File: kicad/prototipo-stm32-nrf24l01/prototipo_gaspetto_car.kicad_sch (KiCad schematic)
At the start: 11 parts, among them J1 Conn_01x07_Pin - TEST POINT, M1 Motor_DC, M2 Motor_DC, Q1 BC548, U1 YAAJ_BluePill_Part_Like_SWD_B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, U2 nRF24L01+, U3 L9110-M1, U4 L9110-M2

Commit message: kicad: clean projects
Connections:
- net at U1.12 (PB4): no longer U2.4 (CSN)
- net at U1.29 (PA4): now also U2.4 (CSN)
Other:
- moved on the sheet: PS1, PS2

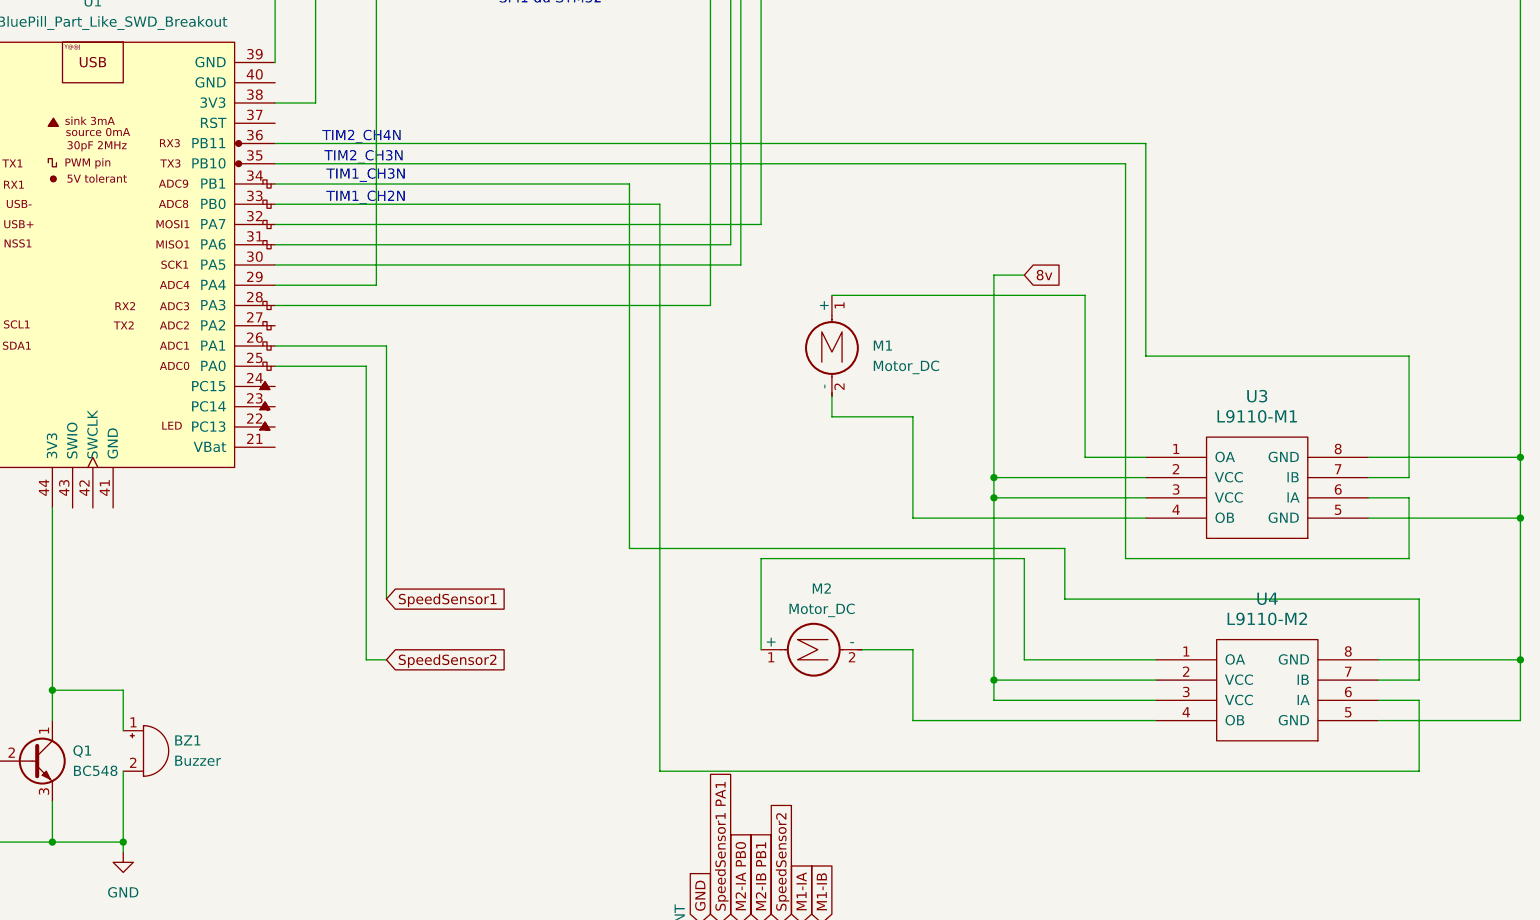
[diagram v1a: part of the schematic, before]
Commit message: sch: gaspetto car match with what's in the board
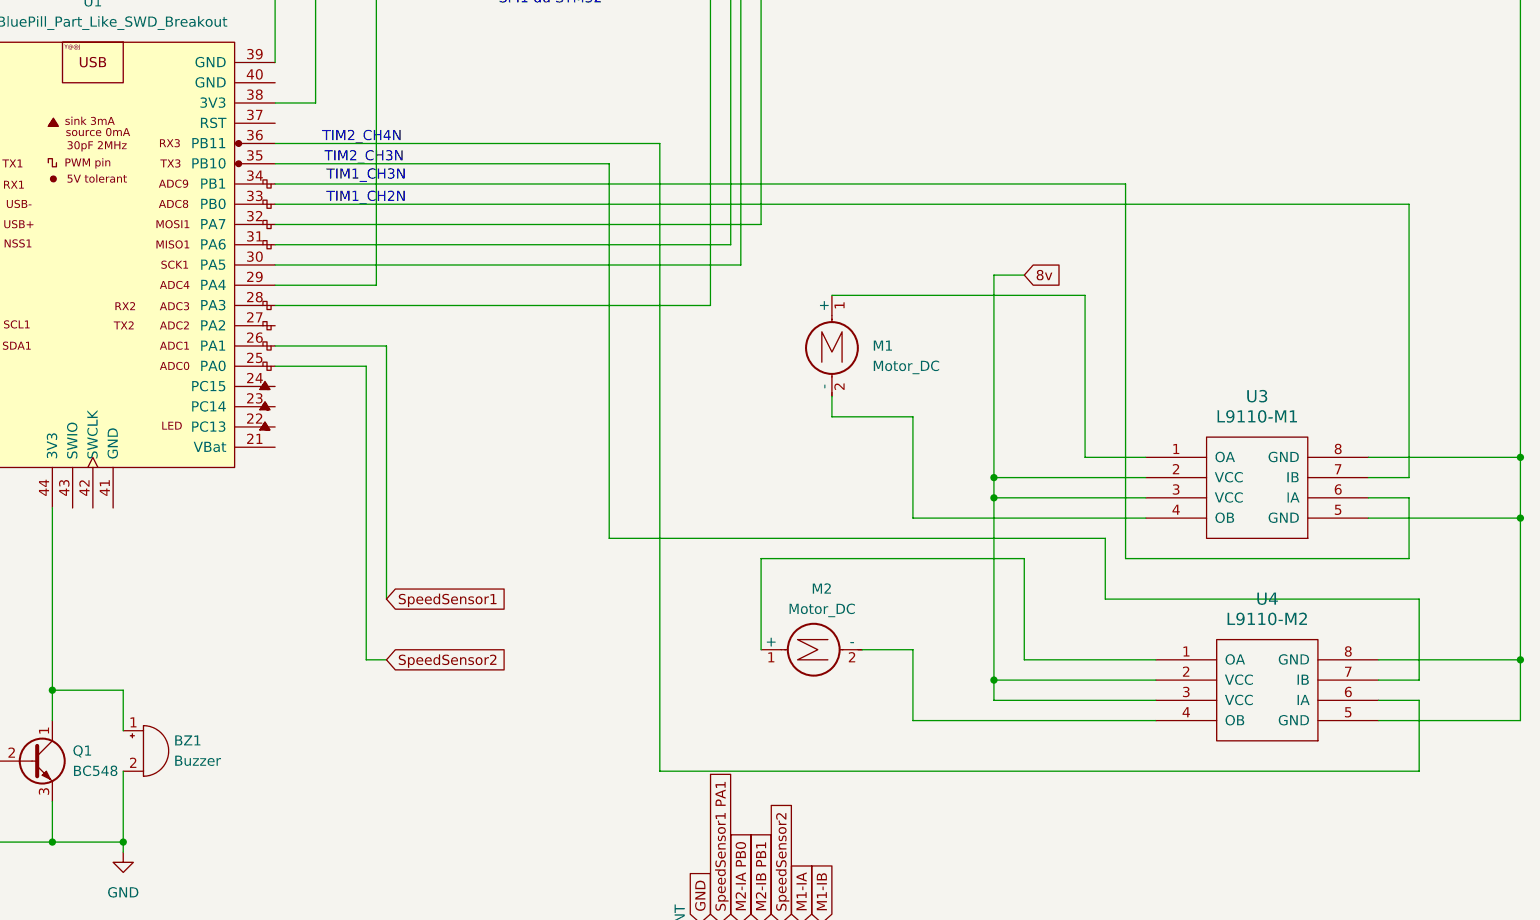
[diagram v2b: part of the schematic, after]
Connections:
- net at U1.33 (PB0): now also U3.7 (IB); no longer U4.6 (IA)
- net at U1.34 (PB1): now also U3.6 (IA); no longer U4.7 (IB)
- net at U1.35 (PB10): now also U4.7 (IB); no longer U3.6 (IA)
- net at U1.36 (PB11): now also U4.6 (IA); no longer U3.7 (IB)

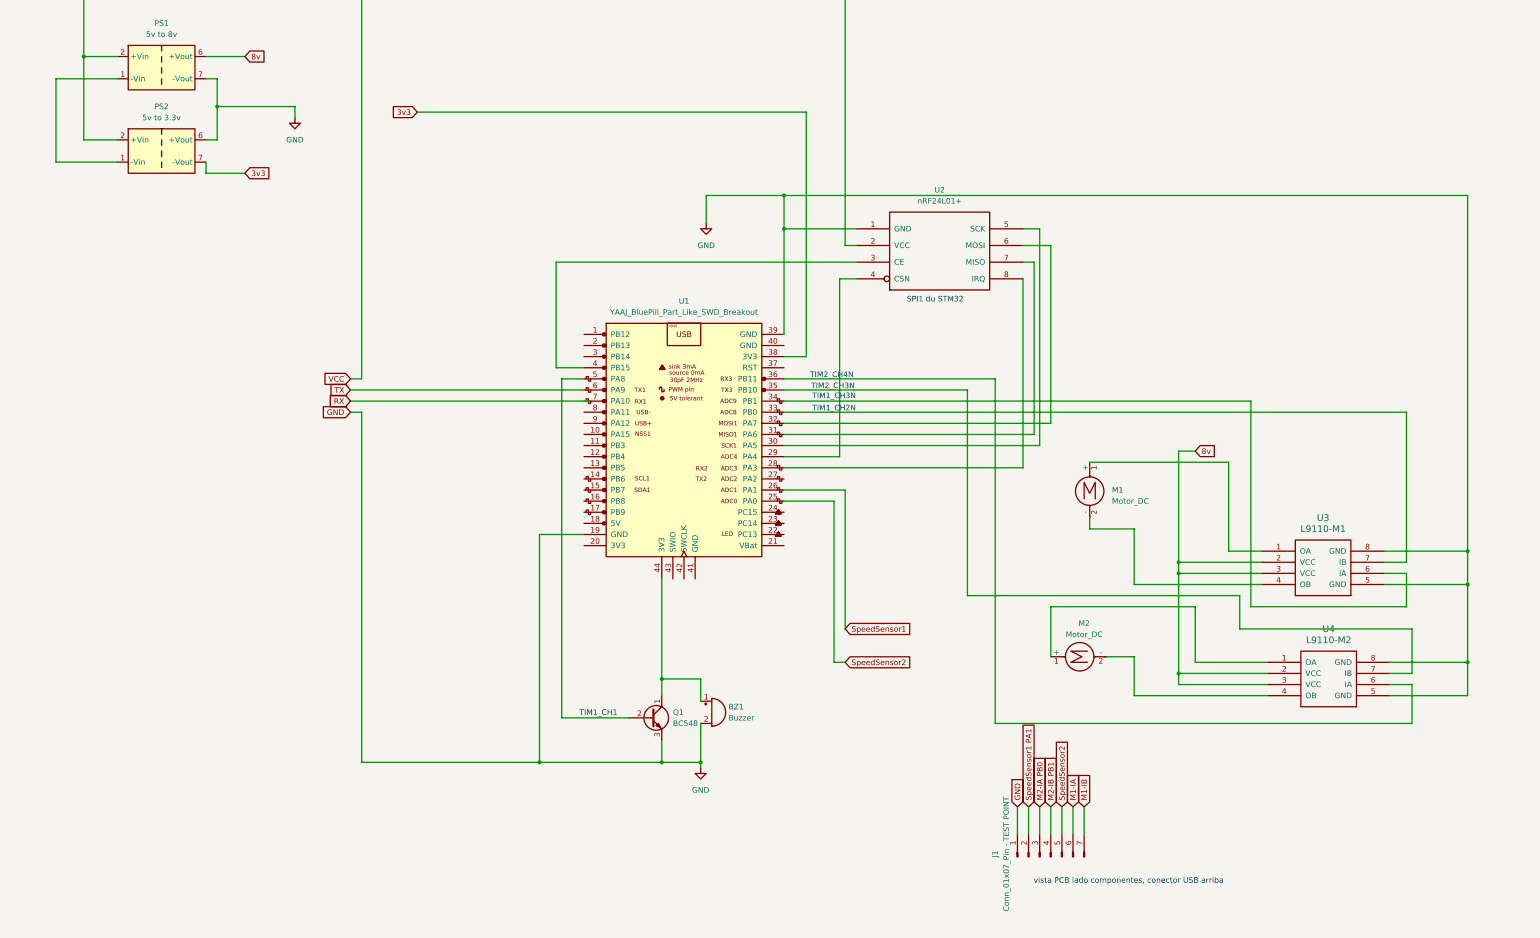
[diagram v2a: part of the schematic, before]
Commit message: sch car: update schematic
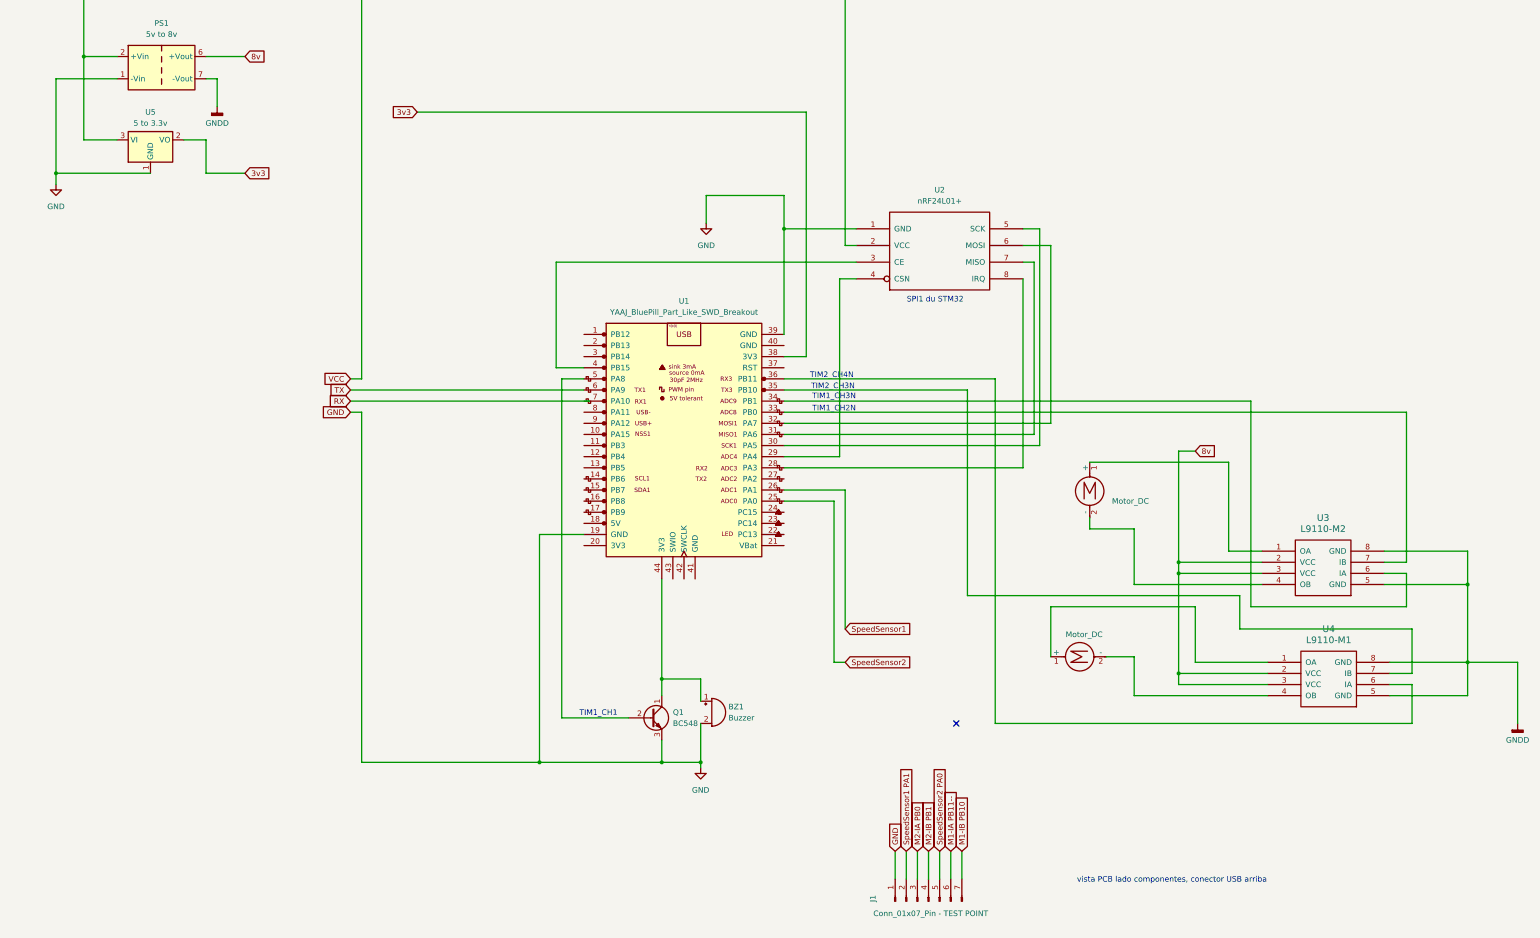
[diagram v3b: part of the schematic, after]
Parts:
- removed PS2: 5v to 3.3v, Converter_DCDC:Converter_DCDC_XP_POWER-ITXxxxxSA_THT, symbol Converter_DCDC:ITX1205SA-H
- added U5: 5 to 3.3v, Package_TO_SOT_SMD:SOT-223-3_TabPin2, symbol Regulator_Linear:LD1117S12TR_SOT223
- U3: value L9110-M1 -> L9110-M2
- U4: value L9110-M2 -> L9110-M1
- renumbered M2 to M1, M1 to M2
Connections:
- net 3v3: now also U5.2 (VO)
- net 5v: now also U5.3 (VI)
- net GND: now also PS1.1 (-Vin), U5.1 (GND); no longer PS1.7 (-Vout), U3.5 (GND), U3.8 (GND), U4.5 (GND), U4.8 (GND)
- net SpeedSensor2: no longer J1.5 (Pin_5)
- net M1-IA renamed M1-IA PB11--
- net M1-IB renamed M1-IB PB10
- new net GNDD: PS1.7 (-Vout), U3.5 (GND), U3.8 (GND), U4.5 (GND), U4.8 (GND)
- new net SpeedSensor2 PA0: J1.5 (Pin_5)
- no-connect marks 0 -> 1
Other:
- moved on the sheet: J1
